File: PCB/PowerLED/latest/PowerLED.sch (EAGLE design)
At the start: 0 parts

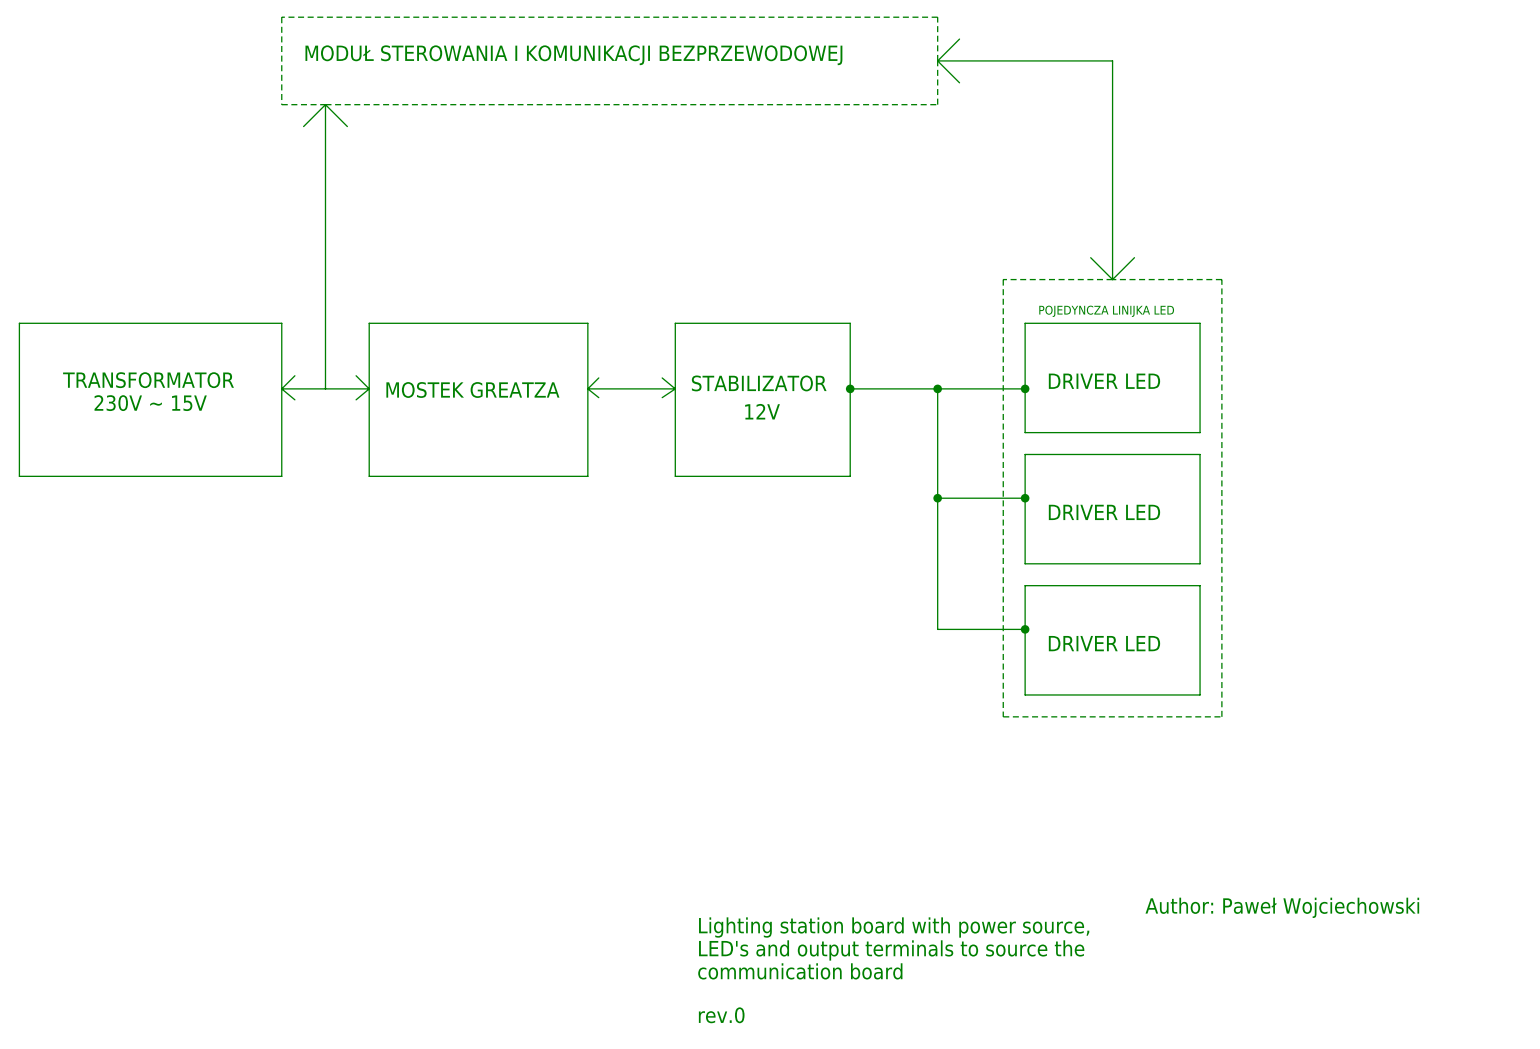
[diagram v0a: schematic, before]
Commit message: Poprawienie schematu blokowego
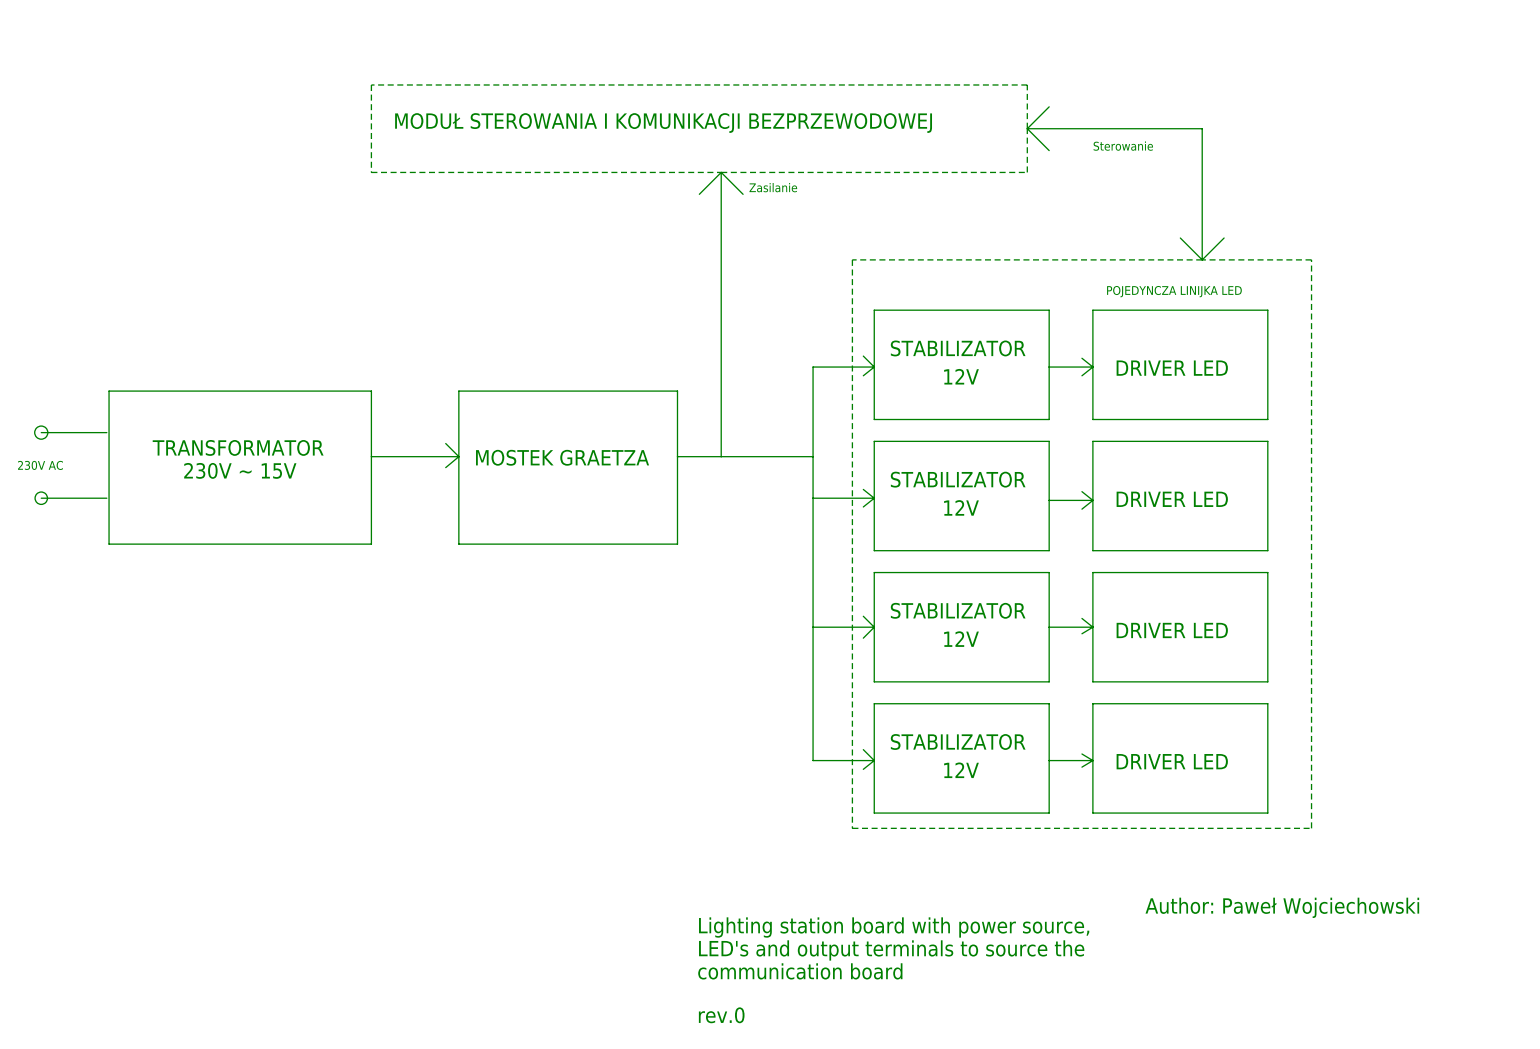
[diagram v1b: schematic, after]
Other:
- note added: "230V AC"
- note added: "MOSTEK GRAETZA"
- note added: "Sterowanie"
- note added: "Zasilanie"
- note removed: "MOSTEK GREATZA"

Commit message: Kosmetyczne poprawki
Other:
- note added: "BLOCK DIAGRAM"
- note added: "MAIN"
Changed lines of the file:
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@@
 <parts>
 <part name="FRAME1" library="frames" library_urn="urn:adsk.eagle:library:229" deviceset="DINA5_L" device=""/>
+<part name="FRAME2" library="frames" library_urn="urn:adsk.eagle:library:229" deviceset="A4L-LOC" device=""/>
 </parts>
 <sheets>
 <sheet>
 <plain>
-<text x="78.74" y="0" size="1.778" layer="91">Lighting station board with power source,
+<text x="78.74" y="2.032" size="1.778" layer="91">Lighting station board with power source,
 LED's and output terminals to source the
 communication board</text>
-<text x="130.81" y="7.62" size="1.778" layer="91">Author: Paweł Wojciechowski</text>
+<text x="78.74" y="-1.778" size="1.778" layer="91">Author: Paweł Wojciechowski</text>
 <text x="78.74" y="-5.08" size="1.778" layer="91">rev.0</text>
 <text x="15.494" y="58.166" size="1.778" layer="91">TRANSFORMATOR
@@
 <text x="101.092" y="72.39" size="1.778" layer="91">STABILIZATOR</text>
 <text x="107.188" y="69.088" size="1.778" layer="91">12V</text>
+<text x="130.556" y="7.62" size="2.54" layer="91">BLOCK DIAGRAM</text>
 </plain>
 <instances>
@@
 </nets>
 </sheet>
+<sheet>
+<plain>
+<text x="217.17" y="20.32" size="2.54" layer="91">MAIN</text>
+<text x="164.084" y="14.224" size="1.778" layer="91">Lighting station board with power source,
+LED's and output terminals to source the
+communication board</text>
+<text x="164.084" y="10.414" size="1.778" layer="91">Author: Paweł Wojciechowski</text>
+<text x="164.084" y="7.112" size="1.778" layer="91">rev.0</text>
+</plain>
+<instances>
+<instance part="FRAME2" gate="G$1" x="0" y="0" smashed="yes">
+<attribute name="DRAWING_NAME" x="217.17" y="15.24" size="2.54" layer="94"/>
+<attribute name="LAST_DATE_TIME" x="217.17" y="10.16" size="2.286" layer="94"/>
+<attribute name="SHEET" x="230.505" y="5.08" size="2.54" layer="94"/>
+</instance>
+</instances>
+<busses>
+</busses>
+<nets>
+</nets>
+</sheet>
